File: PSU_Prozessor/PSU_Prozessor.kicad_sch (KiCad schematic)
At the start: 85 parts, among them IC1 6N138S, J1 ACJS-MHOP, J3 FC68148S, J4 USB2066-05-RBHM-15-STB-00-01-A, J7 USB2066-05-RBHM-15-STB-00-01-A, Q1 BC847, Q2 2N7002, Q3 BC847, Q4 2N7002, Q5 BC847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

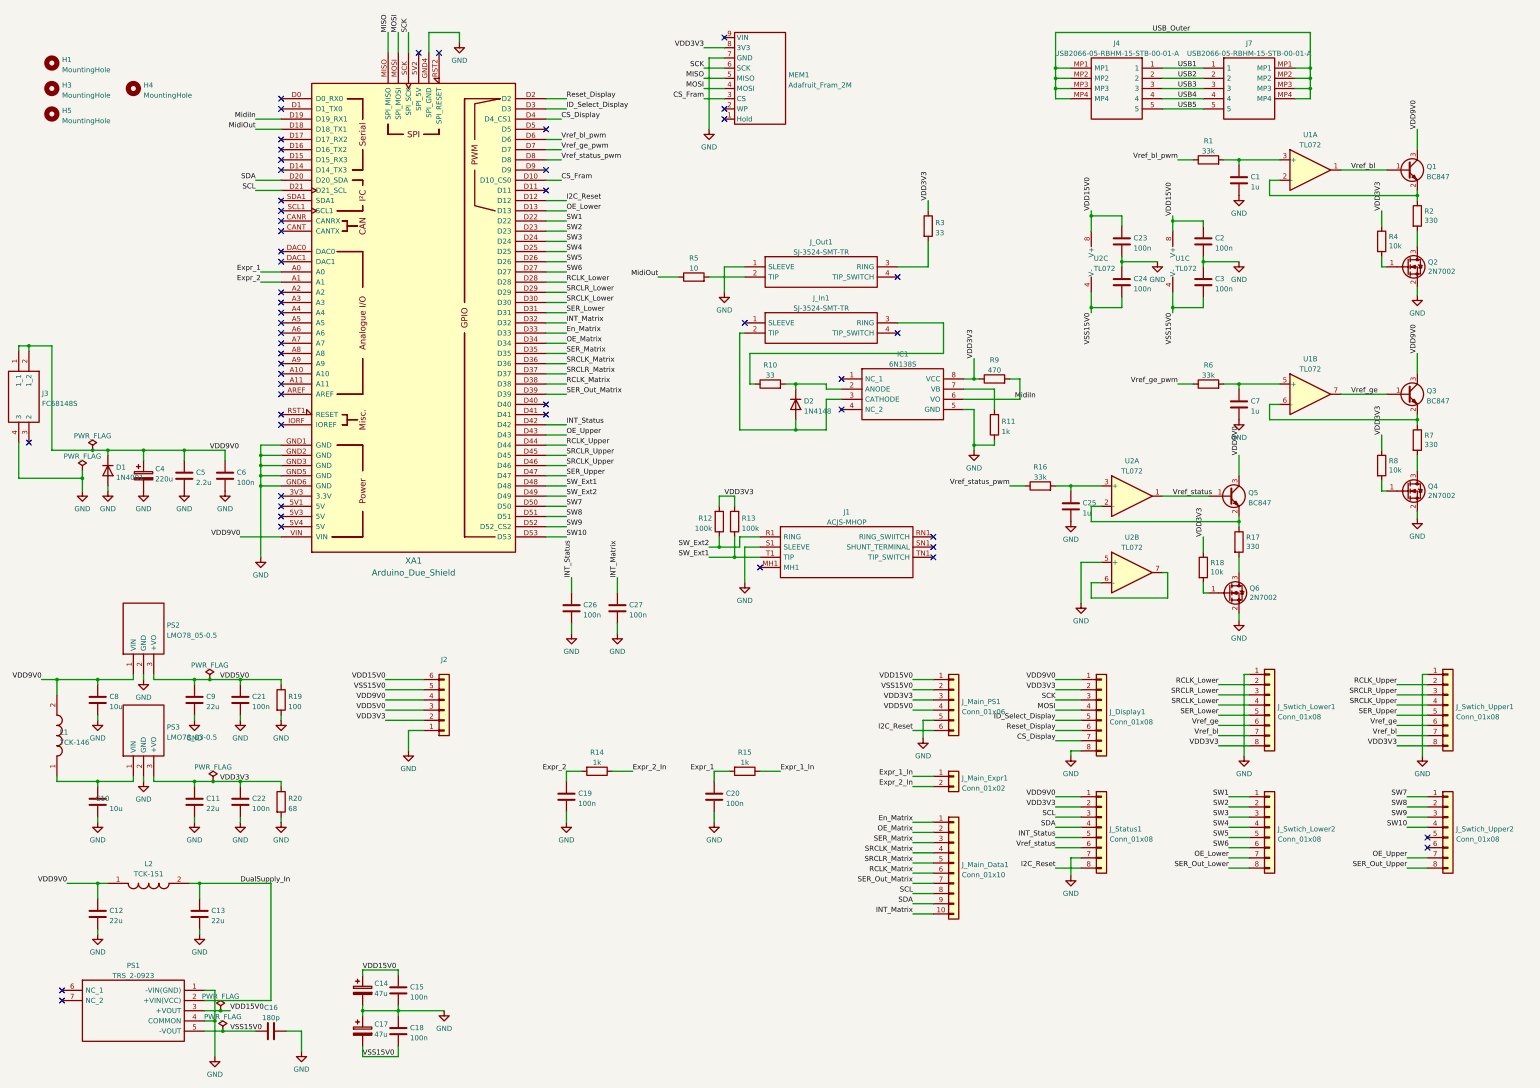
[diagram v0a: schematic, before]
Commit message: Added 9V supply on PSU for LEDs on switch. Changed FRAM supply
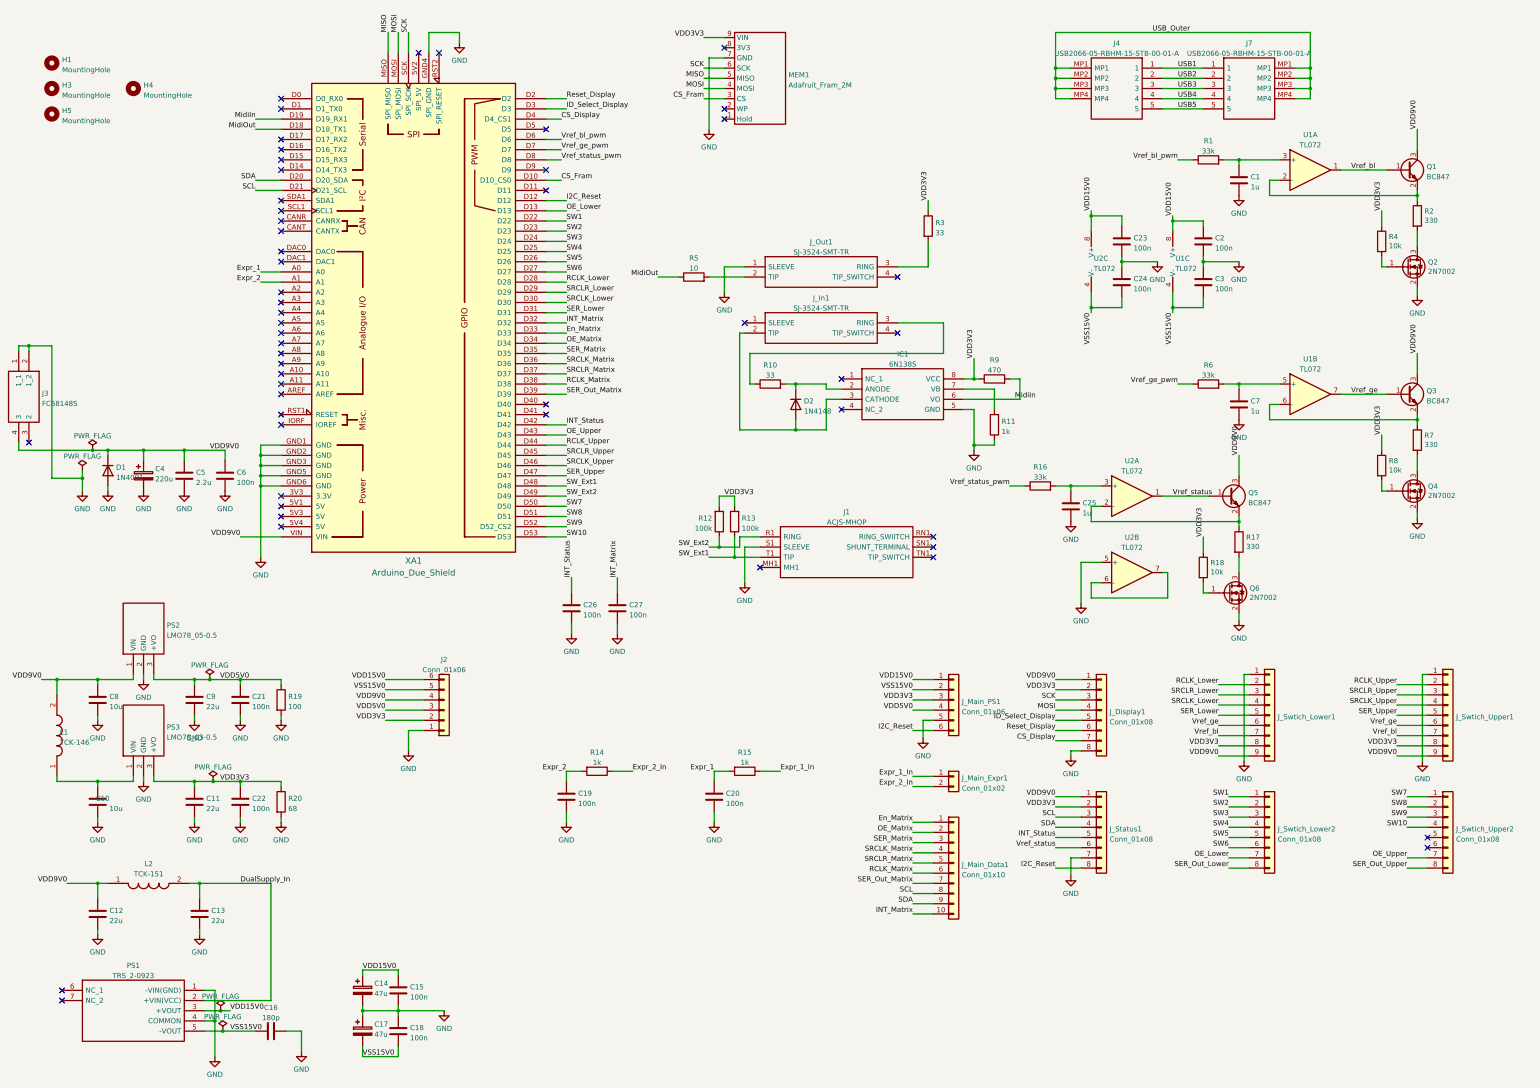
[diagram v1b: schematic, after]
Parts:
- J2: value (none) -> Conn_01x06; footprint (none) -> Connector_PinHeader_2.54mm:PinHeader_1x06_P2.54mm_Vertical
- J4, J7: footprint (none) -> SamacSys_Parts:USB206605RBHM15STB0001A
- J_Swtich_Lower1, J_Swtich_Upper1: value Conn_01x08 -> (none); footprint Connector_JST:JST_PH_B8B-PH-K_1x08_P2.00mm_Vertical -> (none); symbol Connector_Generic:Conn_01x08 -> Connector_Generic:Conn_01x09
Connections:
- net GND: now also J3.1 (1_1), J3.2 (1_2); no longer J3.4 (3)
- net VDD3V3: now also MEM1.9 (VIN); no longer MEM1.8 (3V3)
- net VDD9V0: now also J3.4 (3), J_Swtich_Lower1.9 (Pin_9), J_Swtich_Upper1.9 (Pin_9); no longer J3.1 (1_1), J3.2 (1_2)

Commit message: Changed PSU_Processor PCB to adapt changes on Main PCB
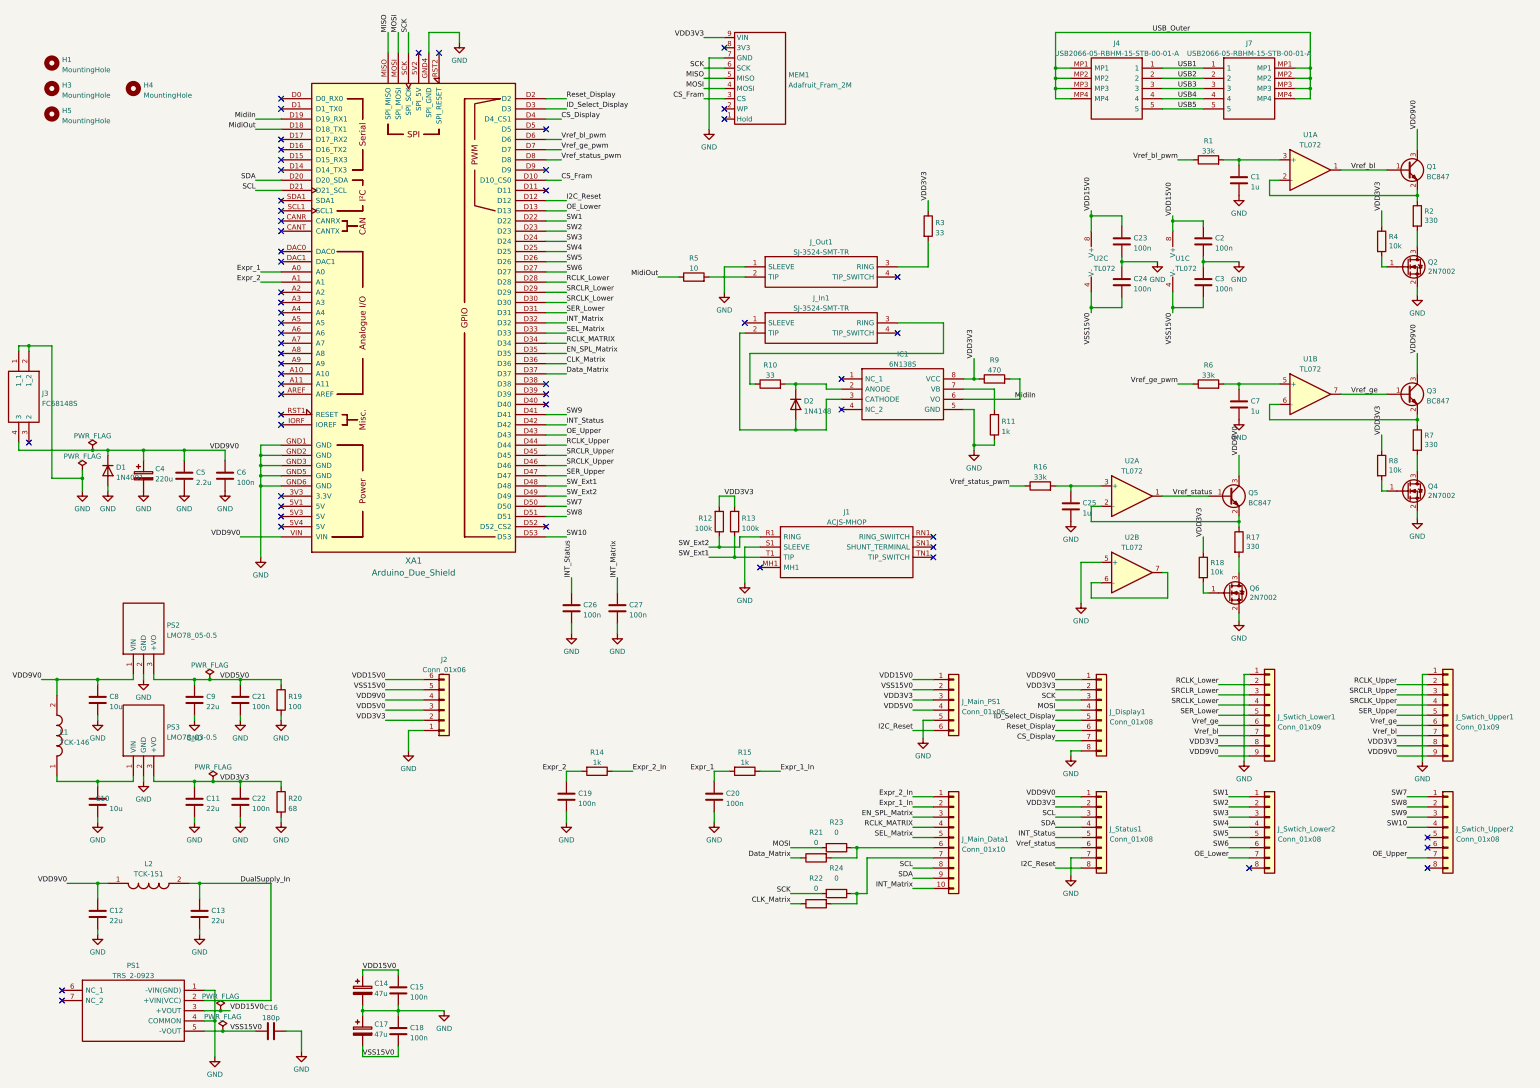
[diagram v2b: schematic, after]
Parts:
- removed J_Main_Expr1: Conn_01x02, Connector_JST:JST_PH_B2B-PH-K_1x02_P2.00mm_Vertical, symbol Connector_Generic:Conn_01x02
- added R21, R22, R23, R24: 0, Resistor_SMD:R_1206_3216Metric_Pad1.30x1.75mm_HandSolder, symbol Device:R
- D2: footprint Diode_SMD:D_SOD-123 -> Diode_THT:D_DO-35_SOD27_P7.62mm_Horizontal
- IC1: footprint SamacSys_Parts:SOP254P1016X460-8N -> SOP254P1016X460-8N
- J1: footprint SamacSys_Parts:ACJSMHOP -> ACJSMHOP
- J3: footprint SamacSys_Parts:FC68148S_2 -> FC68148S_2
- J4, J7: footprint SamacSys_Parts:USB206605RBHM15STB0001A -> USB206605RBHM15STB0001A
- J_In1, J_Out1: footprint SamacSys_Parts:SJ-3524-SMT-TR -> SJ-3524-SMT-TR
- J_Swtich_Lower1, J_Swtich_Upper1: value (none) -> Conn_01x09; footprint (none) -> Connector_JST:JST_PH_B9B-PH-K_1x09_P2.00mm_Vertical
- L1: footprint SamacSys_Parts:TCK147 -> TCK147
- L2: footprint SamacSys_Parts:TCK151 -> TCK151
- PS1: footprint SamacSys_Parts:TRS20922 -> TRS20922
- PS2, PS3: footprint SamacSys_Parts:LMO78_0505 -> LMO78_0505
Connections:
- net Expr_1_In: now also J_Main_Data1.2 (Pin_2)
- net Expr_2_In: now also J_Main_Data1.1 (Pin_1)
- net MOSI: now also R23.2
- net SCK: now also R24.2
- net SW9: now also XA1.D41; no longer XA1.D52 (D52_CS2)
- net En_Matrix renamed SEL_Matrix
- net SEL_Matrix: now also J_Main_Data1.5 (Pin_5); no longer J_Main_Data1.1 (Pin_1)
- net OE_Matrix renamed RCLK_MATRIX
- net RCLK_MATRIX: now also J_Main_Data1.4 (Pin_4); no longer J_Main_Data1.2 (Pin_2)
- net RCLK_Matrix: no longer names the net of J_Main_Data1.6 (Pin_6)
- net RCLK_Matrix: now also R21.2, R23.1; no longer XA1.D38
- net SER_Matrix renamed EN_SPL_Matrix
- net SER_Out_Lower: no longer names the net of J_Swtich_Lower2.8 (Pin_8)
- net SER_Out_Matrix: no longer names the net of J_Main_Data1.7 (Pin_7)
- net SER_Out_Matrix: now also R22.2, R24.1; no longer XA1.D39
- net SER_Out_Upper: no longer names the net of J_Swtich_Upper2.8 (Pin_8)
- net SRCLK_Matrix renamed CLK_Matrix
- net CLK_Matrix: now also R22.1; no longer J_Main_Data1.4 (Pin_4)
- net SRCLR_Matrix renamed Data_Matrix
- net Data_Matrix: now also R21.1; no longer J_Main_Data1.5 (Pin_5)
- no-connect marks 53 -> 57
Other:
- moved on the sheet: J_Main_Data1

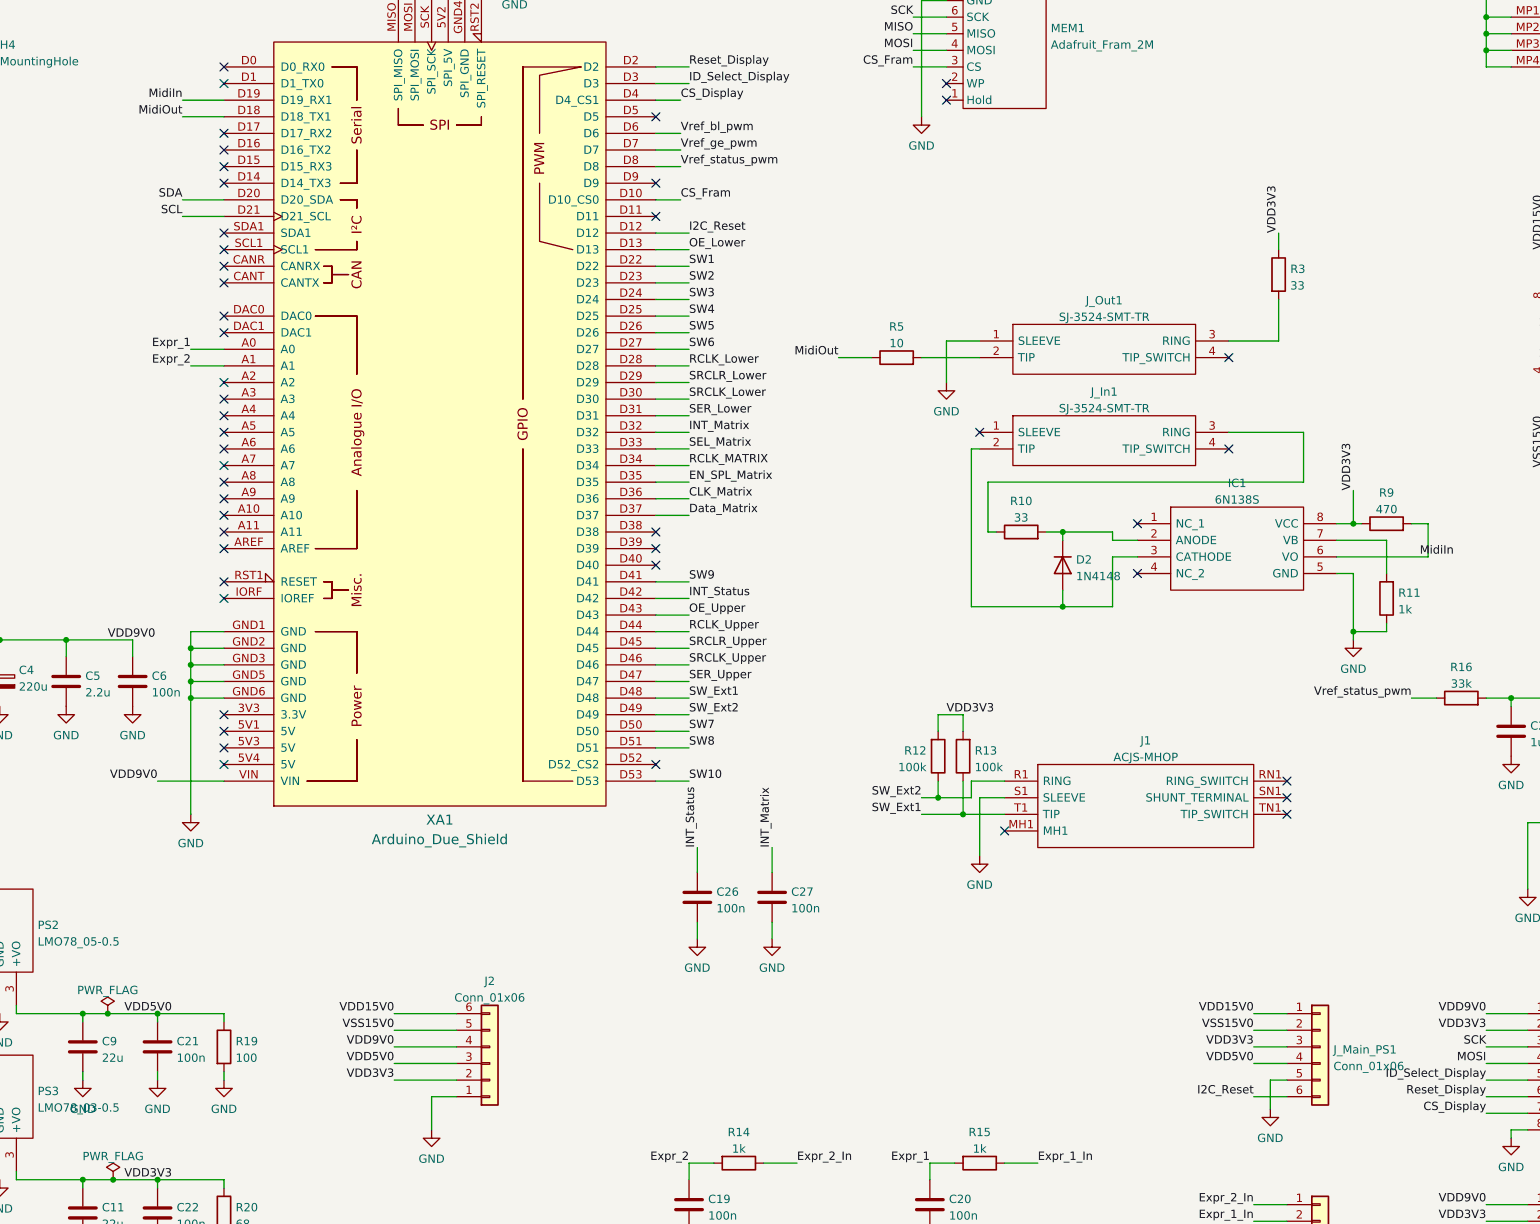
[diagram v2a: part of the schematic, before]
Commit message: Added chip select for amps on main pcb
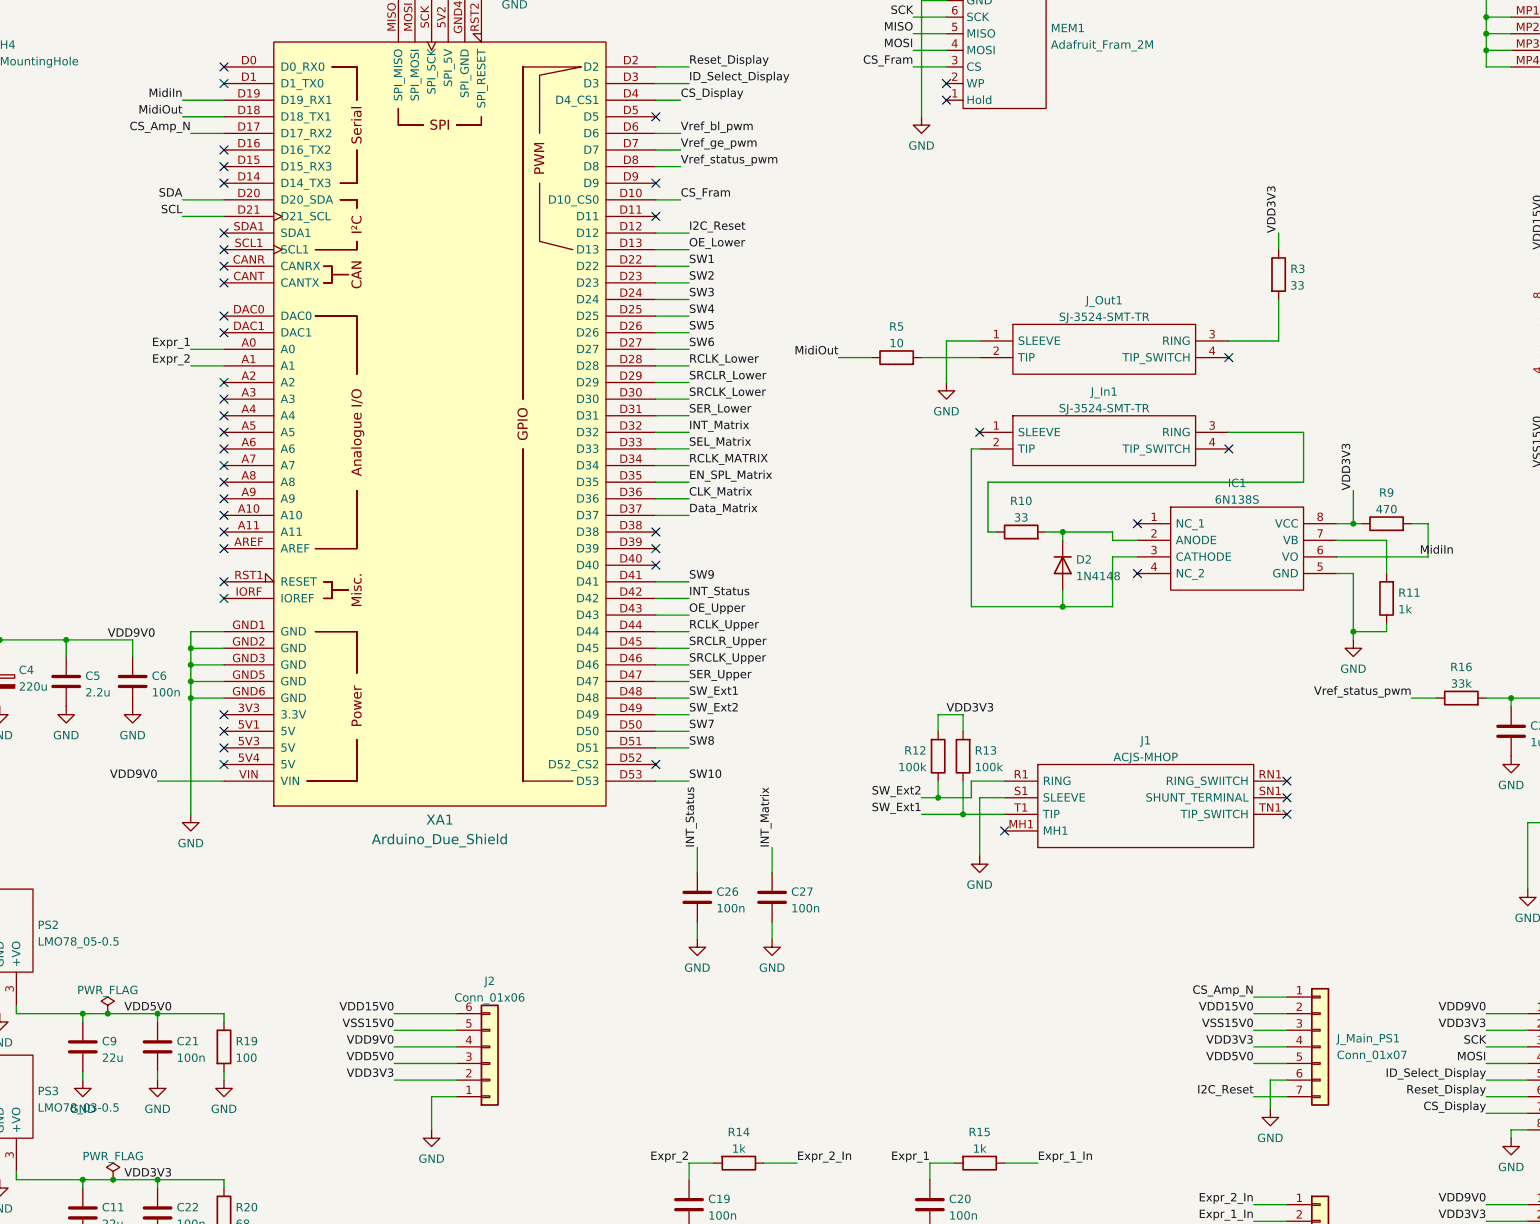
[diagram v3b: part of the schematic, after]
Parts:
- removed J_Main_PS1: Conn_01x06, Connector_JST:JST_PH_B6B-PH-K_1x06_P2.00mm_Vertical, symbol Connector_Generic:Conn_01x06
- added J_Main_PS1: Conn_01x07, Connector_JST:JST_PH_B7B-PH-K_1x07_P2.00mm_Vertical, symbol Connector_Generic:Conn_01x07
- IC1: footprint SOP254P1016X460-8N -> SamacSys_Parts:SOP254P1016X460-8N
- J1: footprint ACJSMHOP -> SamacSys_Parts:ACJSMHOP
- J3: footprint FC68148S_2 -> SamacSys_Parts:FC68148S_2
- J4, J7: footprint USB206605RBHM15STB0001A -> SamacSys_Parts:USB206605RBHM15STB0001A
- J_In1, J_Out1: footprint SJ-3524-SMT-TR -> SamacSys_Parts:SJ-3524-SMT-TR
- L1: footprint TCK147 -> SamacSys_Parts:TCK147
- L2: footprint TCK151 -> SamacSys_Parts:TCK151
- PS1: footprint TRS20922 -> SamacSys_Parts:TRS20922
- PS2, PS3: footprint LMO78_0505 -> SamacSys_Parts:LMO78_0505
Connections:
- net GND: now also J_Main_PS1.6 (Pin_6)
- net I2C_Reset: now also J_Main_PS1.7 (Pin_7)
- net VDD15V0: now also J_Main_PS1.2 (Pin_2)
- net VDD3V3: now also J_Main_PS1.4 (Pin_4)
- net VDD5V0: now also J_Main_PS1.5 (Pin_5)
- net VSS15V0: now also J_Main_PS1.3 (Pin_3)
- net CS_Amp_N: now reaches XA1.D17 (D17_RX2)
- net CS_Amp_N: now also J_Main_PS1.1 (Pin_1)
- no-connect marks 57 -> 56
